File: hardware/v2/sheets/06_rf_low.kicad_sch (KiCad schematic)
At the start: 22 parts, among them J50 RF_LOW_0.1_2.5GHz, T50 2450BL15B0200001E, U50 GRF4001, U51 ADL5801ACPZ-R7

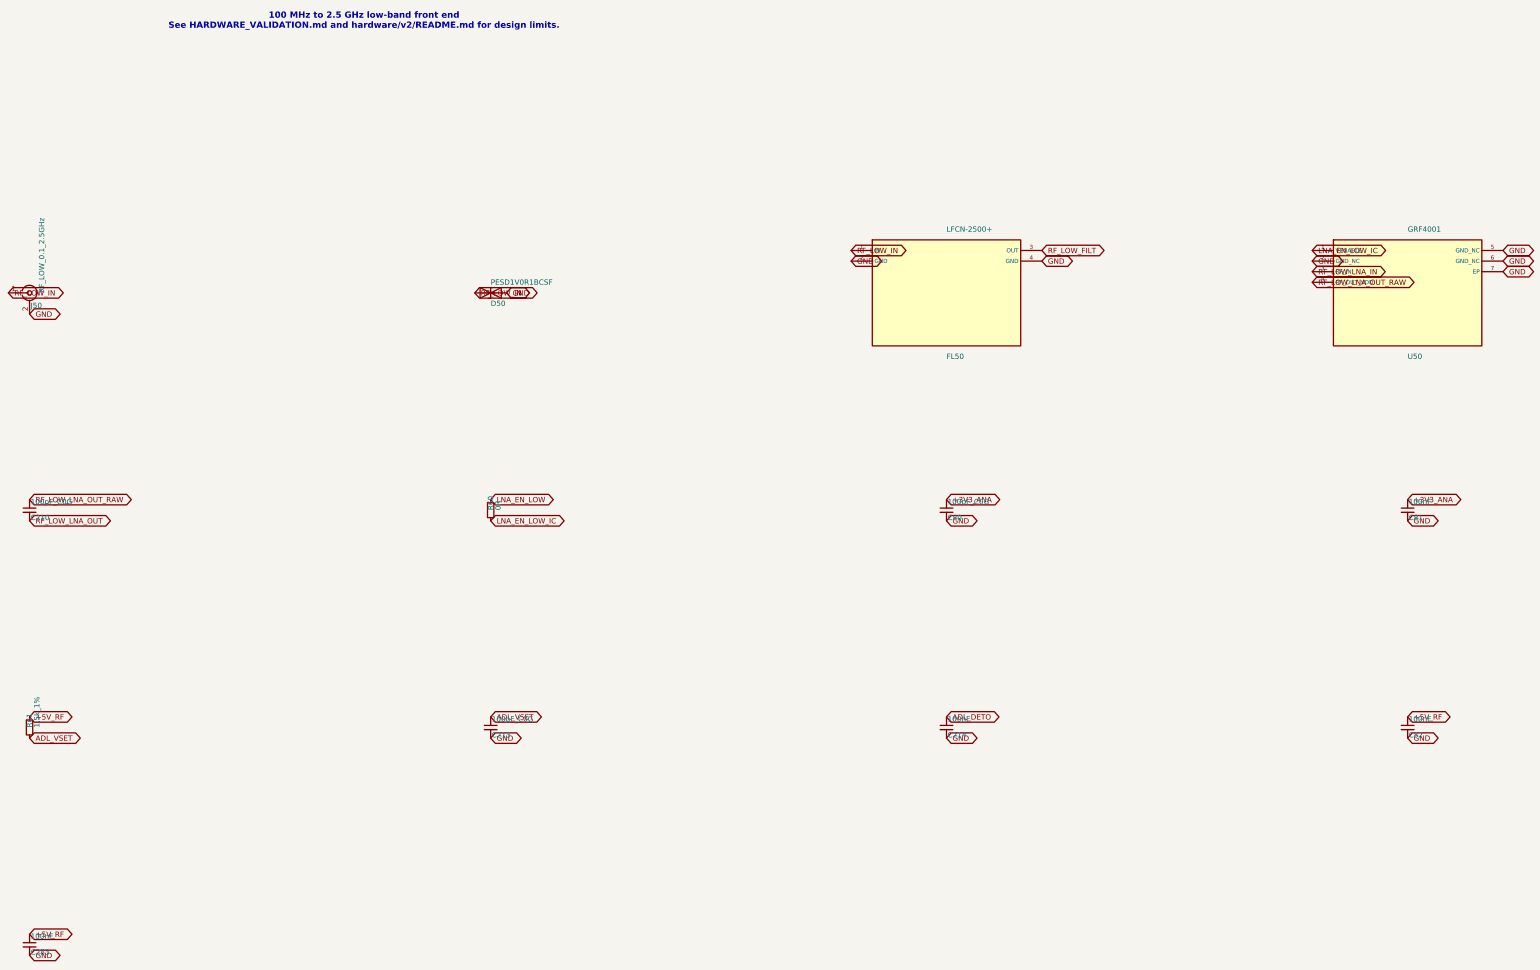
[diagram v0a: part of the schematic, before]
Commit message: hardware: checkpoint corrected V2 routing at 108 opens
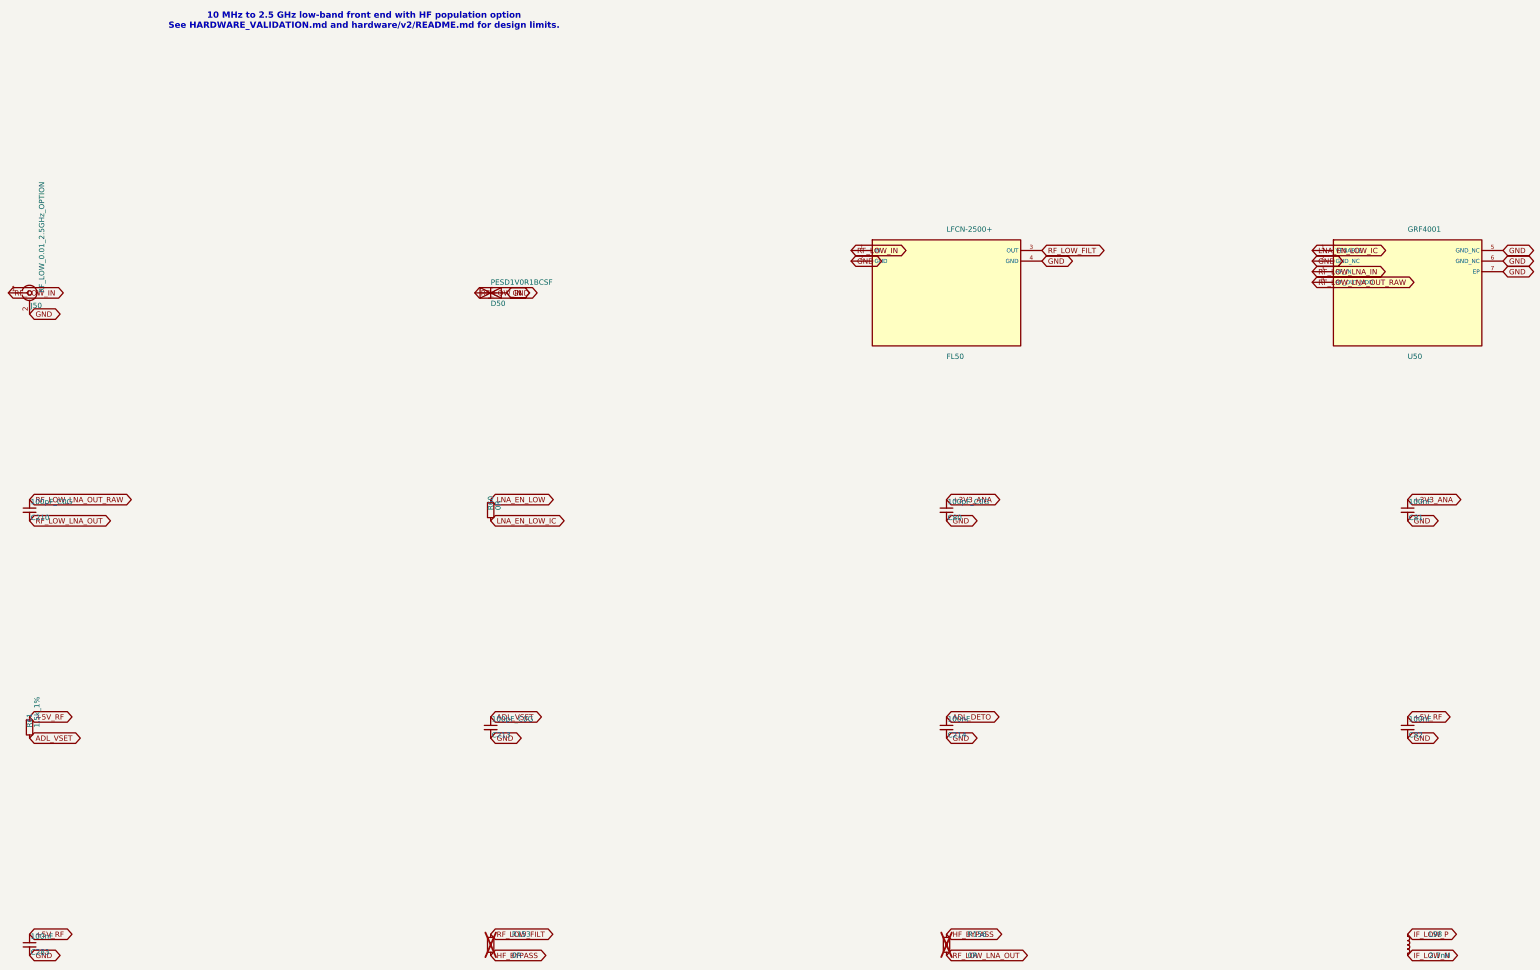
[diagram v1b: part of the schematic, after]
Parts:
- added L98: 2.7nH, Inductor_SMD:L_0402_1005Metric, symbol Device:L_Small
- added R153, R156: 0R, Resistor_SMD:R_0402_1005Metric, symbol Device:R_Small
- J50: value RF_LOW_0.1_2.5GHz -> RF_LOW_0.01_2.5GHz_OPTION
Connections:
- net IF_LOW_N: now also L98.2
- net IF_LOW_P: now also L98.1
- net RF_LOW_FILT: now also R153.1
- net RF_LOW_LNA_OUT: now also R156.2
- new net HF_BYPASS: R153.2, R156.1
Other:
- note added: "10 MHz to 2.5 GHz low-band front end with HF population option See HARDWARE_VALIDATION.md and hardware/v2/README.md for design limits."
- note removed: "100 MHz to 2.5 GHz low-band front end See HARDWARE_VALIDATION.md and hardware/v2/README.md for design limits."
- title: 06 - 100 MHz to 2.5 GHz low-band front end -> 06 - 10 MHz to 2.5 GHz low-band front end with HF population option
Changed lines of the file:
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@@
 	(paper "A1")
 	(title_block
-		(title "06 - 100 MHz to 2.5 GHz low-band front end")
+		(title "06 - 10 MHz to 2.5 GHz low-band front end with HF population option")
 		(rev "2.0")
 		(company "Code-SDR")
@@
 			)
 		)
-		(property "Value" "RF_LOW_0.1_2.5GHz"
+		(property "Value" "RF_LOW_0.01_2.5GHz_OPTION"
 			(at 72.771 90.17 90)
 			(effects
@@
 			)
 		)
-		(property "Description" "Dedicated 100 MHz to 2.5 GHz edge-launch RF input"
+		(property "Description" "100 MHz-2.5 GHz amplified input; optional passive HF population extends coverage to 10 MHz"
 			(at 69.85 90.17 0)
 			(effects
@@
 			)
 		)
-		(property "Description" "LTCC low-pass preselector; 0.1-2.5 GHz receive path"
+		(property "Description" "LTCC low-pass preselector specified DC-2.5 GHz; shared by amplified and passive HF populations"
 			(at 289.56 90.17 0)
 			(effects
@@
 			)
 		)
-		(property "Description" "Low-band first mixer; differential 2.43625 GHz IF"
+		(property "Description" "Low-band first mixer; differential 2.42625 GHz IF"
 			(at 510.54 142.24 0)
 			(effects
@@
 		(at 642.62 189.23)
 	)
-	(text "100 MHz to 2.5 GHz low-band front end\nSee HARDWARE_VALIDATION.md and hardware/v2/README.md for design limits."
+	(text "10 MHz to 2.5 GHz low-band front end with HF population option\nSee HARDWARE_VALIDATION.md and hardware/v2/README.md for design limits."
 		(exclude_from_sim no)
 		(at 150 25 0.0000)
@@
 		)
 	)
+	(symbol (lib_id "Device:R_Small") (at 180.3400 246.3800 0) (unit 1)
+	(exclude_from_sim no) (in_bom yes) (on_board yes)
+	(dnp yes)
+	(fields_autoplaced no)
+	(property "Reference" "R153" (at 185.4200 243.8400 0) (effects (font (size 1.27 1.27)) (justify left)))
+	(property "Value" "0R" (at 185.4200 248.9200 0) (effects (font (size 1.27 1.27)) (justify left)))
+	(property "Footprint" "Resistor_SMD:R_0402_1005Metric" (at 185.4200 248.9200 0) (effects (font (size 1.27 1.27)) (justify left) (hide yes)))
+	(property "Datasheet" "" (at 185.4200 248.9200 0) (effects (font (size 1.27 1.27)) (justify left) (hide yes)))
+	(property "Description" "HF option only: fit R153/R156, omit C208/C210, disable U50. Passive 10 MHz-2.5 GHz coverage trades LNA gain/noise performance for bandwidth. Both endpoint links are omitted in the standard amplified population." (at 185.4200 248.9200 0) (effects (font (size 1.27 1.27)) (justify left) (hide yes)))
+	(pin "1")
+	(pin "2")
+	(instances (project "Code-SDR-V2" (path "/b04744a4-fe39-4740-81de-d5e094f9e157/9f4cb928-74e2-4548-bd64-90561ef0b956" (reference "R153") (unit 1))))
 )
+	(symbol (lib_id "Device:R_Small") (at 289.5600 246.3800 0) (unit 1)
+	(exclude_from_sim no) (in_bom yes) (on_board yes)
+	(dnp yes)
+	(fields_autoplaced no)
+	(property "Reference" "R156" (at 294.6400 243.8400 0) (effects (font (size 1.27 1.27)) (justify left)))
+	(property "Value" "0R" (at 294.6400 248.9200 0) (effects (font (size 1.27 1.27)) (justify left)))
+	(property "Footprint" "Resistor_SMD:R_0402_1005Metric" (at 294.6400 248.9200 0) (effects (font (size 1.27 1.27)) (justify left) (hide yes)))
+	(property "Datasheet" "" (at 294.6400 248.9200 0) (effects (font (size 1.27 1.27)) (justify left) (hide yes)))
+	(property "Description" "HF option only: fit R153/R156, omit C208/C210, disable U50. Passive 10 MHz-2.5 GHz coverage trades LNA gain/noise performance for bandwidth. Both endpoint links are omitted in the standard amplified population." (at 294.6400 248.9200 0) (effects (font (size 1.27 1.27)) (justify left) (hide yes)))
+	(pin "1")
+	(pin "2")
+	(instances (project "Code-SDR-V2" (path "/b04744a4-fe39-4740-81de-d5e094f9e157/9f4cb928-74e2-4548-bd64-90561ef0b956" (reference "R156") (unit 1))))
+)
+	(symbol (lib_id "Device:L_Small") (at 400.0500 246.3800 0) (unit 1)
+	(exclude_from_sim no) (in_bom yes) (on_board yes)
+	(dnp no)
+	(fields_autoplaced no)
+	(property "Reference" "L98" (at 405.1300 243.8400 0) (effects (font (size 1.27 1.27)) (justify left)))
+	(property "Value" "2.7nH" (at 405.1300 248.9200 0) (effects (font (size 1.27 1.27)) (justify left)))
+	(property "Footprint" "Inductor_SMD:L_0402_1005Metric" (at 405.1300 248.9200 0) (effects (font (size 1.27 1.27)) (justify left) (hide yes)))
+	(property "Datasheet" "" (at 405.1300 248.9200 0) (effects (font (size 1.27 1.27)) (justify left) (hide yes)))
+	(property "Description" "ADL5801 Figure 99 differential shunt L3; Coilcraft 0402HP-2N7XGRW starting value; tune on actual board" (at 405.1300 248.9200 0) (effects (font (size 1.27 1.27)) (justify left) (hide yes)))
+	(pin "1")
+	(pin "2")
+	(instances (project "Code-SDR-V2" (path "/b04744a4-fe39-4740-81de-d5e094f9e157/9f4cb928-74e2-4548-bd64-90561ef0b956" (reference "L98") (unit 1))))
+)
+	(global_label "RF_LOW_FILT" (shape bidirectional) (at 180.3400 243.8400 0) (fields_autoplaced yes) (effects (font (size 1.27 1.27)) (justify left)) (property "Intersheetrefs" "${INTERSHEET_REFS}" (at 182.8800 243.8400 0) (effects (font (size 1.27 1.27)) (justify left) (hide yes))))
+	(global_label "HF_BYPASS" (shape bidirectional) (at 180.3400 248.9200 0) (fields_autoplaced yes) (effects (font (size 1.27 1.27)) (justify left)) (property "Intersheetrefs" "${INTERSHEET_REFS}" (at 182.8800 248.9200 0) (effects (font (size 1.27 1.27)) (justify left) (hide yes))))
+	(global_label "HF_BYPASS" (shape bidirectional) (at 289.5600 243.8400 0) (fields_autoplaced yes) (effects (font (size 1.27 1.27)) (justify left)) (property "Intersheetrefs" "${INTERSHEET_REFS}" (at 292.1000 243.8400 0) (effects (font (size 1.27 1.27)) (justify left) (hide yes))))
+	(global_label "RF_LOW_LNA_OUT" (shape bidirectional) (at 289.5600 248.9200 0) (fields_autoplaced yes) (effects (font (size 1.27 1.27)) (justify left)) (property "Intersheetrefs" "${INTERSHEET_REFS}" (at 292.1000 248.9200 0) (effects (font (size 1.27 1.27)) (justify left) (hide yes))))
+	(global_label "IF_LOW_P" (shape bidirectional) (at 400.0500 243.8400 0) (fields_autoplaced yes) (effects (font (size 1.27 1.27)) (justify left)) (property "Intersheetrefs" "${INTERSHEET_REFS}" (at 402.5900 243.8400 0) (effects (font (size 1.27 1.27)) (justify left) (hide yes))))
+	(global_label "IF_LOW_N" (shape bidirectional) (at 400.0500 248.9200 0) (fields_autoplaced yes) (effects (font (size 1.27 1.27)) (justify left)) (property "Intersheetrefs" "${INTERSHEET_REFS}" (at 402.5900 248.9200 0) (effects (font (size 1.27 1.27)) (justify left) (hide yes))))
+)
